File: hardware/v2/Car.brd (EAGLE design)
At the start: 83.8 x 55.9 mm, 72 parts

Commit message: More updates to schematic and layout. Checkpointing.
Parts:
- removed C11, C9, PSB2: 1u, rcl:C0805
- removed CA, CB: 1n, rcl:C0805
- removed RA, RB, RFA, RFB, RGA, RGB: 2k, rcl:R0805
- removed U$1, U$2: MCP6L2-X_SN, microchip2:SOIC8-N_MC
- added C6, C7, C8: 1u, rcl:C1206
- added M1_CA, M1_CB, M2_CA, M2_CB: 100nF, rcl:C0805
- added M1_LPF, M1_LPF1: MCP6L2-X_SN, microchip2:SOIC8-N_MC
- added M1_R1A, M1_R1B, M2_R1A, M2_R1B: 105k, rcl:R0805
- added M1_R2A, M1_R2B, M2_R2A, M2_R2B: 200k, rcl:R0805
- added M1_RA, M1_RB, M2_RA, M2_RB: 22k, rcl:R0805
- RL1, RL2: value 1k -> 2k
- RN1: value 10k -> 22k
- moved PSB1 24.8 mm to (12.1, 21.6), turned to 90 degrees
- moved C1 22.3 mm to (22.2, 21.6), turned to 90 degrees
- moved SJ1 19.7 mm to (5.08, 27.3)
- moved SJ2 19.7 mm to (5.08, 24.8)
- moved J1 19.7 mm to (5.08, 26.0)
- moved R14 17.6 mm to (4.45, 47.0), turned to 0 degrees
- moved R13 17.1 mm to (8.89, 47.0), turned to 0 degrees
- moved 1LGB 14.5 mm to (44.5, 53.3), turned to 0 degrees
- moved C5 13.3 mm to (51.4, 31.1)
- moved PSB3 12.7 mm to (19.1, 21.6)
- moved HB 12.2 mm to (7.62, 34.9), turned to 90 degrees
- moved R15 11.7 mm to (17.8, 34.9), turned to 0 degrees
- moved RL1 11.0 mm to (3.17, 34.9), turned to 180 degrees
- moved 5V 9.67 mm to (5.71, 41.9), turned to 270 degrees
- moved R16 9.44 mm to (13.3, 34.9), turned to 0 degrees
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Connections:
- removed net VDD: U$2.8
- removed net VSS: U$2.4
- new net N$12: M1_LPF1.3, M2_CA.1, M2_RA.1
- new net N$19: M1_LPF1.2, M2_R1A.2
- new net N$23: M1_LPF1.6, M2_R1B.2
- new net N$24: M1_LPF1.5, M2_CB.1, M2_RB.1
- net 12V: now also C6.1; no longer PSB2.1
- net 3V3: now also C7.1; no longer C9.1
- net 5V: now also C8.1, M1_LPF.8, M1_LPF1.8; no longer C11.1, U$1.8
- net AGND: now also M1_CA.2, M1_CB.2, M1_LPF.4, M1_LPF1.4, M1_R2A.2, M1_R2B.2, M2_CA.2, M2_CB.2, M2_R2A.2, M2_R2B.2; no longer CA.2, CB.2, RGA.2, RGB.2, U$1.4
- net GND: now also C6.2, C7.2, C8.2; no longer C11.2, C9.2, PSB2.2
- net M1_PWM1: now also M1_RA.2; no longer RA.2
- net M1_PWM2: now also M1_RB.2; no longer RB.2
- net M1_V1: now also M1_LPF.1, M1_R1A.1, M1_R2A.1; no longer RFA.1, RGA.1, U$1.1
- net M1_V2: now also M1_LPF.7, M1_R1B.1, M1_R2B.1; no longer RFB.1, RGB.1, U$1.7
- net M2_PWM1: now also M2_RA.2
- net M2_PWM2: now also M2_RB.2
- net M2_V1: now also M1_LPF1.1, M2_R1A.1, M2_R2A.1
- net M2_V2: now also M1_LPF1.7, M2_R1B.1, M2_R2B.1
- net N$21: now also M1_LPF.6, M1_R1B.2; no longer RFB.2, U$1.6
- net N$22: now also M1_CB.1, M1_LPF.5, M1_RB.1; no longer CB.1, RB.1, U$1.5
- net N$3: now also M1_CA.1, M1_LPF.3, M1_RA.1; no longer CA.1, RA.1, U$1.3
- net N$7: now also M1_LPF.2, M1_R1A.2; no longer RFA.2, U$1.2
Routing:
- net D7: track 0.00 -> 25.0 mm, vias 0 -> 1
- net D6: track 0.00 -> 20.9 mm, vias 0 -> 1
- net D5: track 0.00 -> 17.7 mm, vias 0 -> 1
- net D3: track 0.00 -> 17.5 mm, vias 0 -> 1
- net D2: track 0.00 -> 14.8 mm, vias 0 -> 1
- net D4: track 0.00 -> 14.6 mm, vias 0 -> 1
- net D1: track 0.00 -> 12.5 mm, vias 0 -> 1
- net D0: track 0.00 -> 10.0 mm, vias 0 -> 1
- net GND: track 0.00 -> 4.95 mm

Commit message: Checkpointing.
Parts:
- moved RL1 38.4 mm to (36.8, 53.3), turned to 90 degrees
- moved HB 32.4 mm to (34.3, 53.3), turned to 180 degrees
- moved PWR 5.24 mm to (2.54, 33.7), turned to 180 degrees
- moved RL2 2.29 mm to (5.08, 33.7), turned to 90 degrees
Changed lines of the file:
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@@
 </class>
 </classes>
-<designrules name="default">
+<designrules name="default *">
 <description language="en">&lt;b&gt;EAGLE Design Rules&lt;/b&gt;
 &lt;p&gt;
@@
 necessary adjustments and save your customized
 design rules under a new name.</description>
-<param name="layerSetup" value="(1*16)"/>
+<param name="layerSetup" value="(1*2+15*16)"/>
 <param name="mtCopper" value="0.035mm 0.035mm 0.035mm 0.035mm 0.035mm 0.035mm 0.035mm 0.035mm 0.035mm 0.035mm 0.035mm 0.035mm 0.035mm 0.035mm 0.035mm 0.035mm"/>
-<param name="mtIsolate" value="1.5mm 0.15mm 0.2mm 0.15mm 0.2mm 0.15mm 0.2mm 0.15mm 0.2mm 0.15mm 0.2mm 0.15mm 0.2mm 0.15mm 0.2mm"/>
+<param name="mtIsolate" value="0.8mm 0.2mm 0.2mm 0.15mm 0.2mm 0.15mm 0.2mm 0.15mm 0.2mm 0.15mm 0.2mm 0.15mm 0.2mm 0.15mm 0.8mm"/>
 <param name="mdWireWire" value="10mil"/>
 <param name="mdWirePad" value="10mil"/>
@@
 <attribute name="VALUE" x="74.073" y="12.598" size="1.016" layer="27" rot="R90" align="center"/>
 </element>
-<element name="RL1" library="rcl" package="R0805" value="2k" x="3.175" y="34.925" smashed="yes" rot="R180">
-<attribute name="NAME" x="3.175" y="33.401" size="1.016" layer="25" rot="R180" align="center"/>
-<attribute name="VALUE" x="3.213" y="35.366" size="1.016" layer="27" rot="R180" align="center"/>
+<element name="RL1" library="rcl" package="R0805" value="2k" x="36.83" y="53.34" smashed="yes" rot="R90">
+<attribute name="NAME" x="35.306" y="53.34" size="1.016" layer="25" rot="R90" align="center"/>
+<attribute name="VALUE" x="37.271" y="53.302" size="1.016" layer="27" rot="R90" align="center"/>
 </element>
 <element name="21RS" library="resistor" package="R2512" value="1" x="61.595" y="5.08" smashed="yes" rot="R90">
@@
 <attribute name="VALUE" x="61.363" y="41.885" size="1.016" layer="27" rot="R270" align="center"/>
 </element>
-<element name="HB" library="led" package="CHIP-LED0805" value="LED" x="7.62" y="34.925" smashed="yes" rot="R90">
-<attribute name="NAME" x="7.62" y="36.195" size="1.016" layer="25" rot="R180" align="center"/>
+<element name="HB" library="led" package="CHIP-LED0805" value="LED" x="34.29" y="53.34" smashed="yes" rot="R180">
+<attribute name="NAME" x="33.02" y="53.34" size="1.016" layer="25" rot="R270" align="center"/>
 </element>
 <element name="2LDB" library="rcl" package="C0805" value="100n" x="61.595" y="12.7" smashed="yes" rot="R270">
@@
 <attribute name="VALUE" x="6.985" y="50.8" size="1.27" layer="27"/>
 </element>
-<element name="PWR" library="led" package="CHIP-LED0805" value="LED" x="7.62" y="32.385" smashed="yes" rot="R90">
-<attribute name="NAME" x="7.62" y="33.655" size="1.016" layer="25" align="center"/>
-</element>
-<element name="RL2" library="rcl" package="R0805" value="2k" x="3.175" y="32.385" smashed="yes" rot="R180">
-<attribute name="NAME" x="3.175" y="33.909" size="1.016" layer="25" align="center"/>
-<attribute name="VALUE" x="3.175" y="32.004" size="1.016" layer="27" align="center"/>
+<element name="PWR" library="led" package="CHIP-LED0805" value="LED" x="2.54" y="33.655" smashed="yes" rot="R180">
+<attribute name="NAME" x="1.27" y="33.655" size="1.016" layer="25" rot="R90" align="center"/>
+</element>
+<element name="RL2" library="rcl" package="R0805" value="2k" x="5.08" y="33.655" smashed="yes" rot="R90">
+<attribute name="NAME" x="6.604" y="33.655" size="1.016" layer="25" rot="R270" align="center"/>
+<attribute name="VALUE" x="4.699" y="33.655" size="1.016" layer="27" rot="R270" align="center"/>
 </element>
 <element name="1LDC" library="SparkFun-Passives" package="PANASONIC_C" value="100u" x="66.04" y="41.91" smashed="yes" rot="R270">
@@
 <contactref element="HB" pad="C"/>
 <contactref element="RL1" pad="1"/>
-<wire x1="4.125" y1="34.925" x2="6.57" y2="34.925" width="0" layer="19" extent="1-1"/>
+<wire x1="34.29" y1="52.29" x2="36.83" y2="52.39" width="0" layer="19" extent="1-1"/>
 </signal>
 <signal name="PGD">
@@
 <contactref element="PWR" pad="C"/>
 <contactref element="RL2" pad="1"/>
-<wire x1="4.125" y1="32.385" x2="6.57" y2="32.385" width="0" layer="19" extent="1-1"/>
+<wire x1="2.54" y1="32.605" x2="5.08" y2="32.705" width="0" layer="19" extent="1-1"/>
 </signal>
 <signal name="N$11">
@@
 <contactref element="AIO" pad="10"/>
 <contactref element="HB" pad="A"/>
-<wire x1="42.545" y1="32.72" x2="31.115" y2="53.848" width="0" layer="19" extent="1-1"/>
-<wire x1="8.67" y1="34.925" x2="31.115" y2="53.848" width="0" layer="19" extent="1-1"/>
+<wire x1="31.115" y1="53.848" x2="34.29" y2="54.39" width="0" layer="19" extent="1-1"/>
+<wire x1="42.545" y1="32.72" x2="34.29" y2="54.39" width="0" layer="19" extent="1-1"/>
 </signal>
 <signal name="/RST">
@@
 <wire x1="17.275" y1="37.465" x2="18.73" y2="34.925" width="0" layer="19" extent="1-1"/>
 <wire x1="18.339" y1="29.845" x2="18.73" y2="34.925" width="0" layer="19" extent="1-1"/>
-<wire x1="8.67" y1="32.385" x2="17.275" y2="37.465" width="0" layer="19" extent="1-1"/>
-<wire x1="1.778" y1="15.24" x2="8.67" y2="32.385" width="0" layer="19" extent="1-1"/>
+<wire x1="2.54" y1="34.705" x2="17.275" y2="37.465" width="0" layer="19" extent="1-1"/>
+<wire x1="8.255" y1="54.102" x2="17.275" y2="37.465" width="0" layer="19" extent="1-1"/>
+<wire x1="1.778" y1="15.24" x2="2.54" y2="34.705" width="0" layer="19" extent="1-1"/>
 <wire x1="8.255" y1="2.032" x2="1.778" y2="15.24" width="0" layer="19" extent="1-1"/>
 <wire x1="17.78" y1="5.3721" x2="8.255" y2="2.032" width="0" layer="19" extent="1-1"/>
 <wire x1="20.32" y1="5.4" x2="17.78" y2="5.3721" width="0" layer="19" extent="1-1"/>
-<wire x1="8.255" y1="54.102" x2="17.275" y2="37.465" width="0" layer="19" extent="1-1"/>
 </signal>
 <signal name="DGND" class="1">
@@
 <wire x1="49.531" y1="48.532" x2="50.801" y2="48.532" width="0" layer="19" extent="1-1"/>
 <wire x1="45.4" y1="53.34" x2="49.531" y2="48.532" width="0" layer="19" extent="1-1"/>
+<wire x1="36.83" y1="54.29" x2="45.4" y2="53.34" width="0" layer="19" extent="1-1"/>
 <wire x1="45.72" y1="21.91" x2="51.435" y2="32.065" width="0" layer="19" extent="1-1"/>
 <wire x1="42.545" y1="23.16" x2="45.72" y2="21.91" width="0" layer="19" extent="1-1"/>
@@
 <wire x1="20.32" y1="7.3" x2="13.97" y2="14.9479" width="0" layer="19" extent="1-1"/>
 <wire x1="5.842" y1="24.765" x2="7.62" y2="14.9479" width="0" layer="19" extent="1-1"/>
-<wire x1="2.225" y1="34.925" x2="5.842" y2="24.765" width="0" layer="19" extent="1-1"/>
 <wire x1="10.795" y1="1.778" x2="20.32" y2="7.3" width="0" layer="19" extent="1-1"/>
-<wire x1="10.795" y1="53.848" x2="2.225" y2="34.925" width="0" layer="19" extent="1-1"/>
+<wire x1="10.795" y1="53.848" x2="36.83" y2="54.29" width="0" layer="19" extent="1-1"/>
 </signal>
 <signal name="GND" class="1">
@@
 <contactref element="C7" pad="2"/>
 <wire x1="3.495" y1="46.99" x2="5.585" y2="49.53" width="0" layer="19" extent="1-1"/>
-<wire x1="14.475" y1="37.465" x2="3.495" y2="46.99" width="0" layer="19" extent="1-1"/>
-<wire x1="12.385" y1="34.925" x2="14.475" y2="37.465" width="0" layer="19" extent="1-1"/>
-<wire x1="2.225" y1="32.385" x2="12.385" y2="34.925" width="0" layer="19" extent="1-1"/>
-<wire x1="3.81" y1="27.305" x2="2.225" y2="32.385" width="0" layer="19" extent="1-1"/>
+<wire x1="5.08" y1="34.605" x2="3.495" y2="46.99" width="0" layer="19" extent="1-1"/>
+<wire x1="12.385" y1="34.925" x2="5.08" y2="34.605" width="0" layer="19" extent="1-1"/>
+<wire x1="14.475" y1="37.465" x2="12.385" y2="34.925" width="0" layer="19" extent="1-1"/>
+<wire x1="4.318" y1="27.305" x2="5.08" y2="34.605" width="0" layer="19" extent="1-1"/>
 <wire x1="12.265" y1="19.79" x2="4.318" y2="24.765" width="0" layer="19" extent="1-1"/>
 <wire x1="16.51" y1="20.19" x2="12.265" y2="19.79" width="0" layer="19" extent="1-1"/>

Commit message: Started routing pcb for reals.
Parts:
- removed 3V3, 5V: 317EMP, linear:SOT223
- added U$1, U$2: LM317, misc:SOT23
- M1_CA, M1_CB, M2_CA, M2_CB: value 100nF -> 100n
- moved C1 11.3 mm to (33.0, 18.1), turned to 180 degrees
- moved RL1 0.64 mm to (37.5, 53.3)
- moved HB 0.63 mm to (34.9, 53.3)
- turned PWR to 0 degrees
- turned RL2 to 270 degrees
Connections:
- net 12V: now also U$1.3, U$2.3; no longer 3V3.3, 5V.3
- net 3V3: now also U$2.2, U$2.4; no longer 3V3.4
- net 5V: now also U$1.2, U$1.4; no longer 5V.4
- net GND: now also J1.2
- net N$20: now also U$2.1; no longer 3V3.1
- net N$27: now also U$1.1; no longer 5V.1
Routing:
- net AGND: track 0.00 -> 205.3 mm, vias 0 -> 4
- net 12V: track 0.00 -> 55.0 mm, vias 0 -> 2
- net GND: track 4.95 -> 35.6 mm
- net 3V3: track 0.00 -> 14.8 mm
- net DGND: track 0.00 -> 13.8 mm
- net N$27: track 0.00 -> 8.02 mm
- net N$20: track 0.00 -> 6.82 mm
- net 5V: track 0.00 -> 5.98 mm
- net N$40: track 0.00 -> 5.46 mm
- net N$24: track 0.00 -> 5.04 mm
- net N$22: track 0.00 -> 5.04 mm
- net N$35: track 0.00 -> 4.95 mm
- net N$11: track 0.00 -> 3.57 mm
- net N$46: track 0.00 -> 2.64 mm
- net N$65: track 0.00 -> 2.64 mm
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- added copper zone on layer 1, net 3V3
- added copper zone on layer 1, net 5V
- removed copper zone on layer 1, net +3V3
- removed copper zone on layer 1, net +5V
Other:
- board text added: "--"

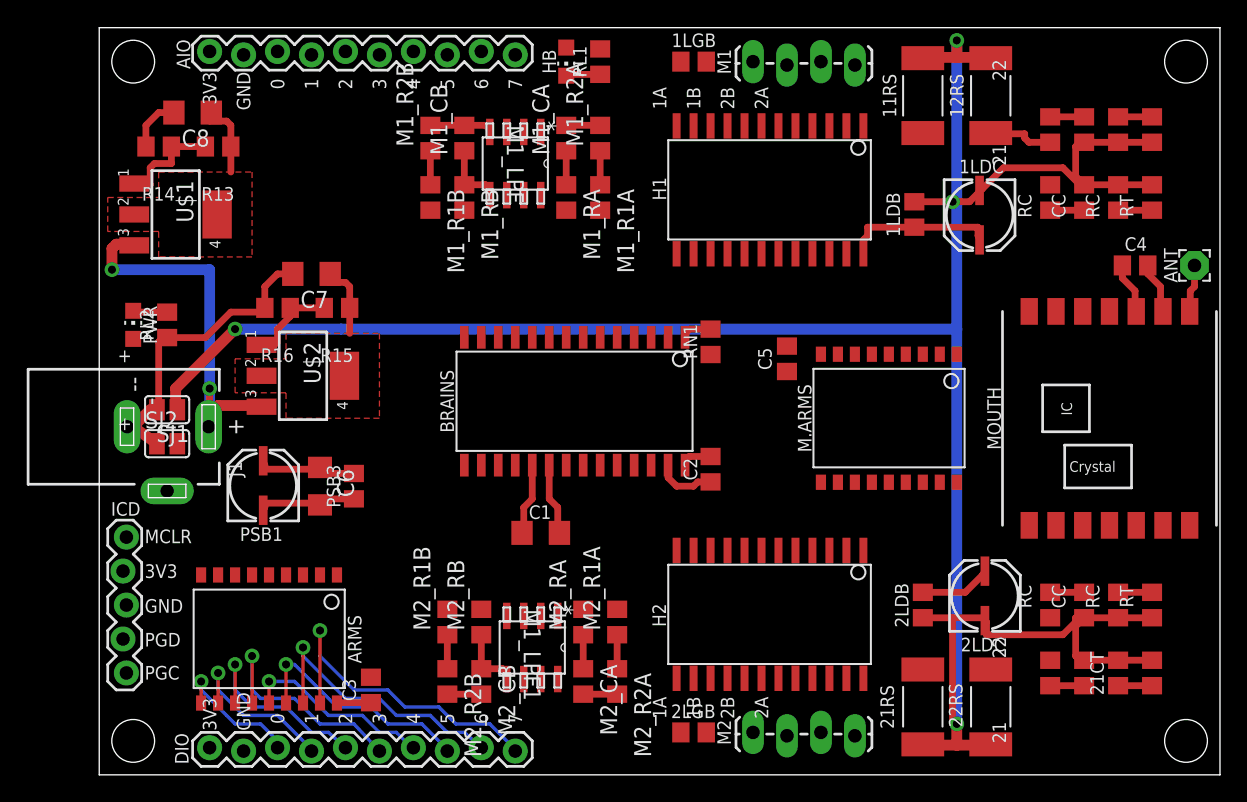
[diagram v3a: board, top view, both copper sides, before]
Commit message: Routed power traces.
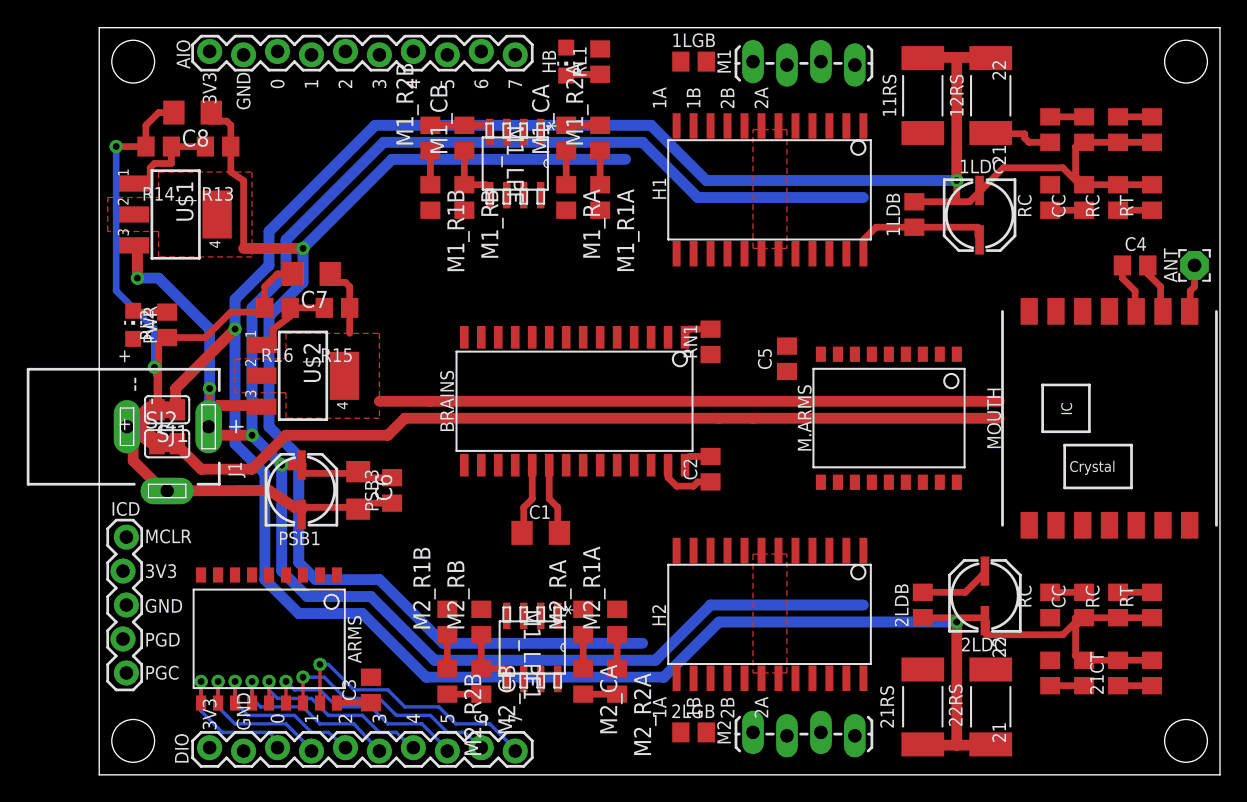
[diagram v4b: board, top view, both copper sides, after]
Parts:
- moved PSB1 2.88 mm to (14.9, 21.3)
- moved C6 2.88 mm to (19.4, 21.3)
- moved PSB3 2.88 mm to (21.9, 21.3)
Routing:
- net 12V: track 55.0 -> 177.1 mm, vias 2 -> 4
- net 5V: track 5.98 -> 97.2 mm, vias 0 -> 1
- net DGND: track 13.8 -> 77.7 mm
- net 3V3: track 14.8 -> 61.2 mm
- net AGND: track 205.3 -> 251.3 mm, vias 4 -> 3
- net GND: track 35.6 -> 75.4 mm, vias 0 -> 2
- net D7: track 25.0 -> 20.2 mm
- net D6: track 20.9 -> 17.4 mm
- net D3: track 17.5 -> 14.1 mm
- net D2: track 14.8 -> 12.8 mm
- net D5: track 17.7 -> 15.9 mm
- net N$25: track 0.00 -> 1.27 mm
- net D0: track 10.0 -> 11.0 mm
- net D1: track 12.5 -> 11.9 mm
- added copper zone on layer 1, net DGND
